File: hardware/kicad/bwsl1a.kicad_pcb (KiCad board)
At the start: 4 copper layers, 160 x 90 mm, 67 parts, among them J1 Conn_01x03, J11 USB_OTG, J13 USB_67298-4090, J14 Conn_02x05_Odd_Even, J17 Molex 470531000, J2 Conn_02x07_Odd_Even, J3 Conn_01x03, J9 THD-02-R, U1 TPD4EUSB30, U11 EMC2301-1-ACZL-TR, U13 FSUSB42MUX, U14 74LVC1G07SE-7, U2 TPD4EUSB30, U3 MagJack-A70-112-331N126, U4 TPD4EUSB30, U5 74LVC1G07SE-7, U6 USB2514B_Bi, U7 AP2553W6, U8 PCF85063AT/AAZ, U9 74LVC1G07SE-7, Y1 24MHz, Y2 X32K768S301

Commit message: initial pcb design
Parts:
- removed J11: USB_OTG, CM4IO:USB_Micro-B_EDAC_UCON00686
- removed J13: USB_67298-4090, CM4IO:MOLEX_USB_67298-4090
- removed J9: THD-02-R, Connector_PinHeader_2.54mm:PinHeader_2x02_P2.54mm_Vertical
- added C12: 0.1uF, Capacitor_SMD:C_0402_1005Metric, F.Cu at (103.2, 120.6)
- added C13: 10uF, Capacitor_SMD:C_0805_2012Metric, F.Cu at (105.1, 120.6)
- added C18: 0.1uF, Capacitor_SMD:C_0402_1005Metric, F.Cu at (107.0, 120.6)
- added C25: 100uF, Capacitor_SMD:C_1210_3225Metric, F.Cu at (100.7, 120.6)
- added C26: 100uF, Capacitor_SMD:C_1210_3225Metric, F.Cu at (188.7, 120.2)
- added C27: 0.1uF, Capacitor_SMD:C_0402_1005Metric, F.Cu at (186.2, 120.2)
- added C28: 10uF, Capacitor_SMD:C_0805_2012Metric, F.Cu at (184.1, 120.2)
- added C29: 0.1uF, Capacitor_SMD:C_0402_1005Metric, F.Cu at (182.1, 120.2)
- added C30: 100uF, Capacitor_SMD:C_1210_3225Metric, F.Cu at (179.6, 120.2)
- added C31: 10u, Capacitor_SMD:C_0805_2012Metric, F.Cu at (195.7, 127.5)
- added C32: 10u, Capacitor_SMD:C_0805_2012Metric, F.Cu at (193.7, 127.5)
- added C33: 10u, Capacitor_SMD:C_0805_2012Metric, F.Cu at (193.7, 131.0)
- added C34: 10u, Capacitor_SMD:C_0805_2012Metric, F.Cu at (195.7, 131.0)
- added C35: 100uF, Capacitor_Tantalum_SMD:CP_EIA-7343-31_Kemet-D, F.Cu at (190.1, 129.3)
- added C36: 10u, Capacitor_SMD:C_0805_2012Metric, F.Cu at (99.3, 131.7)
- added C37: 10u, Capacitor_SMD:C_0805_2012Metric, F.Cu at (171.3, 124.8)
- added C38: 10u, Capacitor_SMD:C_0805_2012Metric, F.Cu at (97.3, 131.7)
- added C39: 10u, Capacitor_SMD:C_0805_2012Metric, F.Cu at (167.8, 126.9)
- added C40: 10u, Capacitor_SMD:C_0805_2012Metric, F.Cu at (99.3, 128.1)
- added C41: 10u, Capacitor_SMD:C_0805_2012Metric, F.Cu at (167.8, 124.8)
- added C42: 10u, Capacitor_SMD:C_0805_2012Metric, F.Cu at (97.3, 128.1)
- added C43: 10u, Capacitor_SMD:C_0805_2012Metric, F.Cu at (171.3, 126.9)
- added C44: 100uF, Capacitor_Tantalum_SMD:CP_EIA-7343-31_Kemet-D, F.Cu at (102.9, 130.4)
- added C45: 100uF, Capacitor_Tantalum_SMD:CP_EIA-7343-31_Kemet-D, F.Cu at (169.7, 121.4)
- added C5: 100uF, Capacitor_SMD:C_1210_3225Metric, F.Cu at (109.6, 120.6)
- added G***: LOGO, Teapot:TeapotLogo, F.Cu at (127.5, 116.5)
- added G***: LOGO, Teapot:TeapotLogo, B.Cu at (186.9, 92.7)
- added G***: LOGO, Teapot:TextLogo_Teapot, B.Cu at (190.4, 98.1)
- added G***: LOGO, Teapot:TextLogo_BWSL1A, B.Cu at (182.6, 97.8)
- added G***: LOGO, Teapot:TextLogo_DataBoard, B.Cu at (186.1, 100.7)
- added H1: MountingHole, MountingHole:MountingHole_3mm_Pad_Via, F.Cu at (92.1, 72.4)
- added H2: MountingHole, MountingHole:MountingHole_3mm_Pad_Via, F.Cu at (198.7, 72.4)
- added H3: MountingHole, MountingHole:MountingHole_3mm_Pad_Via, F.Cu at (198.7, 139.7)
- added H4: MountingHole, MountingHole:MountingHole_3mm_Pad_Via, F.Cu at (92.1, 139.7)
- added J4: 5V, Connector_Wire:SolderWire-0.5sqmm_1x02_P4.8mm_D0.9mm_OD2.3mm, F.Cu at (166.9, 135.1)
- added J5: USB_67298-4090, Teapot:MOLEX_USB_67298-4090, F.Cu at (138.1, 137.9)
- added J6: 12V, Connector_Wire:SolderWire-0.5sqmm_1x02_P4.8mm_D0.9mm_OD2.3mm, F.Cu at (184.5, 128.4)
- added J7: USB_OTG, Teapot:USB_Micro-B_EDAC_UCON00686, F.Cu at (153.1, 145.5)
- added JP1: WL_DISABLE, Jumper:SolderJumper-2_P1.3mm_Open_RoundedPad1.0x1.5mm, F.Cu at (148.3, 74.8)
- added JP2: BT_DISABLE, Jumper:SolderJumper-2_P1.3mm_Open_RoundedPad1.0x1.5mm, F.Cu at (148.3, 78.7)
- added JP3: EEPROM_WP, Jumper:SolderJumper-2_P1.3mm_Open_RoundedPad1.0x1.5mm, F.Cu at (153.4, 90.7)
- added JP4: USB_BOOT, Jumper:SolderJumper-2_P1.3mm_Open_RoundedPad1.0x1.5mm, F.Cu at (148.3, 71.0)
- added R17: 0R, Resistor_SMD:R_0402_1005Metric, F.Cu at (156.3, 82.5)
- added R18: 0R, Resistor_SMD:R_0402_1005Metric, F.Cu at (156.3, 84.6)
- added R22: 0R, Resistor_SMD:R_0402_1005Metric, F.Cu at (156.3, 83.6)
- added R23: 2.2K 1%, Resistor_SMD:R_0402_1005Metric, F.Cu at (156.3, 79.9)
- added R24: 2.2K 1%, Resistor_SMD:R_0402_1005Metric, F.Cu at (156.3, 80.9)
- added R6: 0R, Resistor_SMD:R_0402_1005Metric, F.Cu at (156.3, 87.6)
- added R7: 0R, Resistor_SMD:R_0402_1005Metric, F.Cu at (156.3, 86.6)
- added R9: 0R, Resistor_SMD:R_0402_1005Metric, F.Cu at (156.3, 85.6)
- added SW1: Wake, Button_Switch_SMD:SW_SPST_TL3342, F.Cu at (177.0, 130.9)
- added TP1: ~, TestPoint:TestPoint_Pad_D1.0mm, F.Cu at (178.8, 137.1)
- added TP10: GLOBAL_EN, TestPoint:TestPoint_Pad_D1.0mm, B.Cu at (117.2, 71.6)
- added TP11: GND, TestPoint:TestPoint_Pad_D1.0mm, B.Cu at (137.9, 83.3)
- added TP12: 3.3v, TestPoint:TestPoint_Pad_D1.0mm, B.Cu at (155.7, 76.8)
- added TP13: TXD0, TestPoint:TestPoint_Pad_D1.0mm, B.Cu at (165.2, 80.5)
- added TP14: RXD0, TestPoint:TestPoint_Pad_D1.0mm, B.Cu at (165.1, 82.9)
- added TP15: GND, TestPoint:TestPoint_Pad_D1.0mm, B.Cu at (167.6, 83.7)
- added TP16: GPS_RESET, TestPoint:TestPoint_Pad_D1.0mm, B.Cu at (104.9, 117.4)
- added TP17: GPS_STANDBY, TestPoint:TestPoint_Pad_D1.0mm, B.Cu at (107.5, 117.4)
- added TP18: GPS_RXD, TestPoint:TestPoint_Pad_D1.0mm, B.Cu at (110.0, 117.4)
- added TP19: GPS_TXD, TestPoint:TestPoint_Pad_D1.0mm, B.Cu at (112.5, 117.4)
- added TP2: AIN0, TestPoint:TestPoint_Pad_D1.0mm, B.Cu at (153.7, 65.5)
- added TP20: GND, TestPoint:TestPoint_Pad_D1.0mm, B.Cu at (115.1, 117.4)
- added TP21: 3.3v LoRaWAN, TestPoint:TestPoint_Pad_D1.0mm, F.Cu at (93.0, 134.4)
- added TP22: 3.3v SWARM, TestPoint:TestPoint_Pad_D1.0mm, F.Cu at (193.8, 120.6)
- added TP23: 5v, TestPoint:TestPoint_Pad_D1.0mm, F.Cu at (162.7, 129.0)
- added TP24: 12v, TestPoint:TestPoint_Pad_D1.0mm, F.Cu at (187.6, 135.5)
- added TP25: GND, TestPoint:TestPoint_Pad_D1.0mm, F.Cu at (177.4, 124.2)
- added TP26: GND, TestPoint:TestPoint_Pad_D1.0mm, F.Cu at (94.1, 120.0)
- added TP4: AIN1, TestPoint:TestPoint_Pad_D1.0mm, B.Cu at (153.8, 67.9)
- added TP6: SYNC_IN, TestPoint:TestPoint_Pad_D1.0mm, B.Cu at (155.8, 90.2)
- added TP7: SYNC_OUT, TestPoint:TestPoint_Pad_D1.0mm, B.Cu at (153.5, 89.8)
- added TP8: TV_OUT, TestPoint:TestPoint_Pad_D1.0mm, B.Cu at (132.6, 90.4)
- added TP9: RUN_PG, TestPoint:TestPoint_Pad_D1.0mm, B.Cu at (168.8, 73.4)
- added U10: RAK5146, Teapot:RAK5146, F.Cu at (106.4, 110.4)
- added U12: Swarm_M138, Teapot:Swarm_M138, F.Cu at (183.9, 110.4)
- BT1, C22, C24, C46, D3, R19, R20, U14, U8, Y2: moved to B.Cu
- J1: value Conn_01x03 -> 3.3V LoRaWAN; footprint Connector_PinHeader_2.54mm:PinHeader_1x03_P2.54mm_Vertical -> Connector_Wire:SolderWire-0.5sqmm_1x02_P4.8mm_D0.9mm_OD2.3mm
- J2: value Conn_02x07_Odd_Even -> 3.3V SWARM; footprint Connector_PinHeader_2.54mm:PinHeader_2x07_P2.54mm_Vertical -> Connector_Wire:SolderWire-0.5sqmm_1x02_P4.8mm_D0.9mm_OD2.3mm
- J3: value Conn_01x03 -> BMS I2C; footprint Connector_PinHeader_2.54mm:PinHeader_1x03_P2.54mm_Vertical -> Connector_PinHeader_2.54mm:PinHeader_1x04_P2.54mm_Vertical; moved to B.Cu
- U3: footprint CM4IO:TRJG0926HENL -> Teapot:TRJG0926HENL
- moved J3 84.4 mm to (161.9, 143.5), turned to 0 degrees
- moved J17 79.4 mm to (183.9, 140.6)
- moved J2 77.6 mm to (199.4, 123.2), turned to -90 degrees
- moved C23 71.9 mm to (170.4, 141.6)
- moved U11 71.9 mm to (174.8, 140.7)
- moved R21 71.9 mm to (174.7, 143.4)
- moved U9 59.2 mm to (175.0, 137.1), turned to 0 degrees
- moved C46 46.8 mm to (97.1, 78.3)
- moved Y2 42.3 mm to (105.2, 80.6), turned to -90 degrees
- moved R19 41.3 mm to (112.3, 77.8), turned to 180 degrees
- moved C24 40.6 mm to (112.8, 79.3), turned to 90 degrees
- moved U8 39.3 mm to (99.3, 82.2)
- moved R20 39.2 mm to (112.3, 80.9), turned to 180 degrees
- moved U14 38.0 mm to (112.9, 83.4), turned to -90 degrees
- moved C22 36.9 mm to (110.8, 83.7), turned to 90 degrees
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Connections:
- C10 pad 1: /USB/+3.3v -> /+3.3v
- C11 pad 1: /USB/+3.3v -> /+3.3v
- C14 pad 1: /USB/+3.3v -> /+3.3v
- C15 pad 1: /USB/+3.3v -> /+3.3v
- C2 pad 1: /USB/+5v -> /+5v
- C22 pad 1: /RTC_Fan/+5v -> /+5v
- C23 pad 1: /RTC_Fan/+3.3v -> /+3.3v
- C3 pad 1: /USB/+3.3v -> /+3.3v
- C4 pad 1: /USB/+3.3v -> /+3.3v
- C6 pad 1: /USB/+3.3v -> /+3.3v
- C7 pad 1: /USB/+3.3v -> /+3.3v
- D1 pad 2: /Ethernet/+3.3v -> /+3.3v
- D2 pad 2: /Ethernet/+3.3v -> /+3.3v
- D3 pad 2: /RTC_Fan/+3.3v -> /+3.3v
- J1 pad 1: /Ethernet/GLOBAL_EN -> GND
- J1 pad 2: GND -> /+3.3vL
- J17 pad 2: /RTC_Fan/+12v -> /+12v
- J2 pad 2: /Ethernet/nRPIBOOT -> /+3.3vS
- J3 pad 1: /Ethernet/WL_nDis -> GND
- J3 pad 2: GND -> /SCL1
- J3 pad 3: /Ethernet/BT_nDis -> /SDA1
- Module1 pad 1: (no net) -> GND
- Module1 pad 10: (no net) -> /IO_Ethernet/TRD0_N
- Module1 pad 100: (no net) -> /USB/nEXTRST
- Module1 pad 11: (no net) -> /IO_Ethernet/TRD2_P
- Module1 pad 111: unconnected-(Module1-Pad111) -> /IO_Ethernet/TV_OUT
- Module1 pad 12: (no net) -> /IO_Ethernet/TRD0_P
- Module1 pad 13: (no net) -> GND
- Module1 pad 14: (no net) -> GND
- Module1 pad 15: (no net) -> /IO_Ethernet/ETH_LEDY
- Module1 pad 16: (no net) -> /IO_Ethernet/SYNC_IN
- Module1 pad 17: (no net) -> /IO_Ethernet/ETH_LEDG
- Module1 pad 18: (no net) -> /IO_Ethernet/SYNC_OUT
- Module1 pad 19: (no net) -> unconnected-(Module1-Pad19)
- Module1 pad 2: (no net) -> GND
- Module1 pad 20: (no net) -> /IO_Ethernet/EEPROM_nWP
- Module1 pad 21: (no net) -> Net-(Module1-Pad21)
- Module1 pad 22: (no net) -> GND
- Module1 pad 23: (no net) -> GND
- Module1 pad 24: (no net) -> Net-(Module1-Pad24)
- Module1 pad 25: (no net) -> unconnected-(Module1-Pad25)
- Module1 pad 26: (no net) -> Net-(Module1-Pad26)
- Module1 pad 27: (no net) -> unconnected-(Module1-Pad27)
- Module1 pad 28: (no net) -> Net-(Module1-Pad28)
- Module1 pad 29: (no net) -> unconnected-(Module1-Pad29)
- Module1 pad 3: (no net) -> /IO_Ethernet/TRD3_P
- Module1 pad 30: (no net) -> unconnected-(Module1-Pad30)
- Module1 pad 31: (no net) -> unconnected-(Module1-Pad31)
- Module1 pad 32: (no net) -> GND
- Module1 pad 33: (no net) -> GND
- Module1 pad 34: (no net) -> /SWARM_TXD
- Module1 pad 35: (no net) -> /IO_Ethernet/ID_SC
- Module1 pad 36: (no net) -> /IO_Ethernet/ID_SD
- Module1 pad 37: (no net) -> unconnected-(Module1-Pad37)
- Module1 pad 38: (no net) -> /LORA_SCK
- Module1 pad 39: (no net) -> /LORA_CSN
- Module1 pad 4: (no net) -> /IO_Ethernet/TRD1_P
- Module1 pad 40: (no net) -> /LORA_MISO
- Module1 pad 41: (no net) -> Net-(Module1-Pad41)
- Module1 pad 42: (no net) -> GND
- Module1 pad 43: (no net) -> GND
- Module1 pad 44: (no net) -> /LORA_MOSI
- Module1 pad 45: (no net) -> Net-(Module1-Pad45)
- Module1 pad 46: (no net) -> unconnected-(Module1-Pad46)
- Module1 pad 47: (no net) -> unconnected-(Module1-Pad47)
- Module1 pad 48: (no net) -> unconnected-(Module1-Pad48)
- Module1 pad 49: (no net) -> unconnected-(Module1-Pad49)
- Module1 pad 5: (no net) -> /IO_Ethernet/TRD3_N
- Module1 pad 50: (no net) -> Net-(Module1-Pad50)
- Module1 pad 51: (no net) -> /IO_Ethernet/RXD0
- Module1 pad 52: (no net) -> GND
- Module1 pad 53: (no net) -> GND
- Module1 pad 54: (no net) -> /SWARM_RXD
- Module1 pad 55: (no net) -> /IO_Ethernet/TXD0
- Module1 pad 56: (no net) -> /SCL1
- Module1 pad 57: (no net) -> unconnected-(Module1-Pad57)
- Module1 pad 58: (no net) -> /SDA1
- Module1 pad 59: (no net) -> GND
- Module1 pad 6: (no net) -> /IO_Ethernet/TRD1_N
- Module1 pad 60: (no net) -> GND
- Module1 pad 61: (no net) -> unconnected-(Module1-Pad61)
- Module1 pad 62: (no net) -> unconnected-(Module1-Pad62)
- Module1 pad 63: (no net) -> unconnected-(Module1-Pad63)
- Module1 pad 64: (no net) -> unconnected-(Module1-Pad64)
- Module1 pad 65: (no net) -> GND
- Module1 pad 66: (no net) -> GND
- Module1 pad 67: (no net) -> unconnected-(Module1-Pad67)
- Module1 pad 68: (no net) -> unconnected-(Module1-Pad68)
- Module1 pad 69: (no net) -> unconnected-(Module1-Pad69)
- Module1 pad 7: (no net) -> GND
- Module1 pad 70: (no net) -> unconnected-(Module1-Pad70)
- Module1 pad 71: (no net) -> GND
- Module1 pad 72: (no net) -> unconnected-(Module1-Pad72)
- Module1 pad 73: (no net) -> unconnected-(Module1-Pad73)
- Module1 pad 74: (no net) -> GND
- Module1 pad 75: (no net) -> unconnected-(Module1-Pad75)
- Module1 pad 76: (no net) -> /IO_Ethernet/Reserved
- Module1 pad 77: (no net) -> /+5v
- Module1 pad 78: (no net) -> /IO_Ethernet/GPIO_VREF
- Module1 pad 79: (no net) -> /+5v
- Module1 pad 8: (no net) -> GND
- Module1 pad 80: (no net) -> unconnected-(Module1-Pad80)
- Module1 pad 81: (no net) -> /+5v
- Module1 pad 82: (no net) -> unconnected-(Module1-Pad82)
- Module1 pad 83: (no net) -> /+5v
- Module1 pad 84: (no net) -> /+3.3v
- Module1 pad 85: (no net) -> /+5v
- Module1 pad 86: (no net) -> /+3.3v
- Module1 pad 87: (no net) -> /+5v
- Module1 pad 88: (no net) -> /IO_Ethernet/+1.8v
- Module1 pad 89: (no net) -> /IO_Ethernet/WL_nDis
- Module1 pad 9: (no net) -> /IO_Ethernet/TRD2_N
- Module1 pad 90: (no net) -> /IO_Ethernet/+1.8v
- Module1 pad 91: (no net) -> /IO_Ethernet/BT_nDis
- Module1 pad 92: (no net) -> /IO_Ethernet/RUN_PG
- Module1 pad 93: (no net) -> /IO_Ethernet/nRPIBOOT
- Module1 pad 94: (no net) -> /IO_Ethernet/AIN1
- Module1 pad 95: (no net) -> /IO_Ethernet/nPWR_LED
- Module1 pad 96: (no net) -> /IO_Ethernet/AIN0
- Module1 pad 97: (no net) -> unconnected-(Module1-Pad97)
- Module1 pad 98: (no net) -> GND
- Module1 pad 99: (no net) -> /IO_Ethernet/GLOBAL_EN
- R1 pad 2: Net-(R1-Pad2) -> Net-(Module1-Pad21)
- R19 pad 2: /RTC_Fan/+5v -> /+5v
- R2 pad 2: /Ethernet/ETH_LEDG -> /IO_Ethernet/ETH_LEDG
- R20 pad 2: /RTC_Fan/+5v -> /+5v
- R21 pad 2: /RTC_Fan/+3.3v -> /+3.3v
- R3 pad 2: /Ethernet/ETH_LEDY -> /IO_Ethernet/ETH_LEDY
- R4 pad 1: /Ethernet/+1.8v -> /IO_Ethernet/+1.8v
- R4 pad 2: /Ethernet/GPIO_VREF -> /IO_Ethernet/GPIO_VREF
- R5 pad 1: /Ethernet/+3.3v -> /+3.3v
- R5 pad 2: /Ethernet/GPIO_VREF -> /IO_Ethernet/GPIO_VREF
- R8 pad 1: /USB/USB_OTG_ID -> Net-(J7-Pad1)
- R8 pad 2: Net-(J11-Pad1) -> /USB/USB_OTG_ID
- U1 pad 1: /Ethernet/TRD3_P -> /IO_Ethernet/TRD3_P
- U1 pad 10: unconnected-(U1-Pad10) -> /IO_Ethernet/TRD3_P
- U1 pad 2: /Ethernet/TRD3_N -> /IO_Ethernet/TRD3_N
- U1 pad 4: /Ethernet/TRD2_N -> /IO_Ethernet/TRD2_N
- U1 pad 5: /Ethernet/TRD2_P -> /IO_Ethernet/TRD2_P
- U1 pad 6: unconnected-(U1-Pad6) -> /IO_Ethernet/TRD2_P
- U1 pad 7: unconnected-(U1-Pad7) -> /IO_Ethernet/TRD2_N
- U1 pad 9: unconnected-(U1-Pad9) -> /IO_Ethernet/TRD3_N
- U11 pad 1: /RTC_Fan/SDA -> /SDA1
- U11 pad 2: /RTC_Fan/SCL -> /SCL1
- U11 pad 3: /RTC_Fan/+3.3v -> /+3.3v
- U13 pad 1: /USB/+3.3v -> /+3.3v
- U13 pad 6: /USB/USBH_P -> /USB/USBH_N
- U13 pad 7: /USB/USBH_N -> /USB/USBH_P
- U14 pad 4: /RTC_Fan/GLOBAL_EN -> /IO_Ethernet/GLOBAL_EN
- U14 pad 5: /RTC_Fan/+5v -> /+5v
- U2 pad 1: /Ethernet/TRD1_P -> /IO_Ethernet/TRD1_P
- U2 pad 10: unconnected-(U2-Pad10) -> /IO_Ethernet/TRD1_P
- U2 pad 2: /Ethernet/TRD1_N -> /IO_Ethernet/TRD1_N
- U2 pad 4: /Ethernet/TRD0_N -> /IO_Ethernet/TRD0_N
- U2 pad 5: /Ethernet/TRD0_P -> /IO_Ethernet/TRD0_P
- U2 pad 6: unconnected-(U2-Pad6) -> /IO_Ethernet/TRD0_P
- U2 pad 7: unconnected-(U2-Pad7) -> /IO_Ethernet/TRD0_N
- U2 pad 9: unconnected-(U2-Pad9) -> /IO_Ethernet/TRD1_N
- U3 pad 1: /Ethernet/TRD0_P -> /IO_Ethernet/TRD0_P
- U3 pad 10: /Ethernet/TRD3_N -> /IO_Ethernet/TRD3_N
- U3 pad 11: /Ethernet/TR0_TAP -> /IO_Ethernet/TR0_TAP
- U3 pad 12: /Ethernet/TR1_TAP -> /IO_Ethernet/TR1_TAP
- U3 pad 13: /Ethernet/TR2_TAP -> /IO_Ethernet/TR2_TAP
- U3 pad 14: /Ethernet/TR3_TAP -> /IO_Ethernet/TR3_TAP
- U3 pad 15: /Ethernet/+3.3v -> /+3.3v
- U3 pad 17: /Ethernet/+3.3v -> /+3.3v
- U3 pad 2: /Ethernet/TRD0_N -> /IO_Ethernet/TRD0_N
- U3 pad 3: /Ethernet/TRD1_P -> /IO_Ethernet/TRD1_P
- U3 pad 6: /Ethernet/TRD1_N -> /IO_Ethernet/TRD1_N
- U3 pad 7: /Ethernet/TRD2_P -> /IO_Ethernet/TRD2_P
- U3 pad 8: /Ethernet/TRD2_N -> /IO_Ethernet/TRD2_N
- U3 pad 9: /Ethernet/TRD3_P -> /IO_Ethernet/TRD3_P
- U4 pad 1: unconnected-(U4-Pad1) -> Net-(U4-Pad1)
- U4 pad 10: unconnected-(U4-Pad10) -> Net-(U4-Pad1)
- U4 pad 2: unconnected-(U4-Pad2) -> Net-(U4-Pad2)
- U4 pad 6: unconnected-(U4-Pad6) -> /USB/USBD_P
- U4 pad 7: unconnected-(U4-Pad7) -> /USB/USBD_N
- U4 pad 9: unconnected-(U4-Pad9) -> Net-(U4-Pad2)
- U5 pad 2: /Ethernet/nPWR_LED -> /IO_Ethernet/nPWR_LED
- U5 pad 5: /Ethernet/+3.3v -> /+3.3v
- U6 pad 10: /USB/+3.3v -> /+3.3v
- U6 pad 15: /USB/+3.3v -> /+3.3v
- U6 pad 23: /USB/+3.3v -> /+3.3v
- U6 pad 27: /USB/+3.3v -> /+3.3v
- U6 pad 29: /USB/+3.3v -> /+3.3v
- U6 pad 36: /USB/+3.3v -> /+3.3v
- U6 pad 5: /USB/+3.3v -> /+3.3v
- U7 pad 1: /USB/+5v -> /+5v
- U8 pad 5: /RTC_Fan/SDA -> /SDA1
- U8 pad 6: /RTC_Fan/SCL -> /SCL1
- U9 pad 2: /Ethernet/RUN_PG -> /IO_Ethernet/RUN_PG
- U9 pad 4: Net-(J2-Pad13) -> Net-(SW1-Pad1)
- U9 pad 5: /Ethernet/+5v -> /+5v
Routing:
- net /USB/+3.3v: track 449.6 -> 0.00 mm, vias 23 -> 0
- net /+3.3v: track 0.00 -> 312.9 mm, vias 0 -> 25
- net /RTC_Fan/+5v: track 262.7 -> 0.00 mm, vias 20 -> 0
- net /SCL1: track 0.00 -> 202.6 mm, vias 0 -> 5
- net /RTC_Fan/SCL: track 201.2 -> 0.00 mm, vias 8 -> 0
- net /SDA1: track 0.00 -> 200.2 mm, vias 0 -> 8
- net /Ethernet/GLOBAL_EN: track 196.2 -> 0.00 mm, vias 5 -> 0
- net /RTC_Fan/SDA: track 194.6 -> 0.00 mm, vias 8 -> 0
- net /+5v: track 0.00 -> 188.0 mm, vias 0 -> 13
- net /Ethernet/RUN_PG: track 170.6 -> 0.00 mm, vias 4 -> 0
- net /IO_Ethernet/GLOBAL_EN: track 0.00 -> 135.5 mm, vias 0 -> 5
- net /Ethernet/nPWR_LED: track 128.9 -> 0.00 mm, vias 2 -> 0
- net Net-(R1-Pad2): track 116.6 -> 0.00 mm, vias 4 -> 0
- net /IO_Ethernet/nPWR_LED: track 0.00 -> 113.2 mm, vias 0 -> 4
- net /+3.3vL: track 0.00 -> 101.9 mm
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- added copper zone on In2.Cu, net /+3.3v
- added copper zone on B.Cu, net GND
- added copper zone on F.Cu, net GND
- added copper zone on In1.Cu, net GND
- added copper zone on In2.Cu, net GND
- removed copper zone on In2.Cu, net /USB/+3.3v
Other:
- board size 160 x 90 mm -> 120 x 90 mm
- board text added: "+"
- board text added: "-"
- board text added: "RAK5146 LoRaWAN Concentrator"
- board text added: "SWARM M138 Transceiver"
- board text removed: "Battery CR2032"
- board text removed: "Board thickness : 1.56mm Finished copper weight inners : 1oz Finished copper weight outers : 1oz Board finish : OSP Material type : FR4 Colour of solder resists : Green Colour of silk screens : White Only on the top side Board to : UL94-V0 TG >=130 50R trace width 0.13mm@ 3GHz 90R diff pair width 0.147 spacing 0.253mm @ 2.5GHz 100R diff pair width 0.127 spacing 0.253mm @ 2GHz"
- board text removed: "FAN"
- board text removed: "Fit jumper to disable eMMC Boot"
- board text removed: "Fit jumper to disable writing to EEPROM"
- board text removed: "J3 : nBT_Dis GND"
- board text removed: "PCIe x1"
- board text removed: "POE"
- board text removed: "RUN GLOBAL_EN"
- board text removed: "Rev 5b"
- board text removed: "nWireless_Dis"

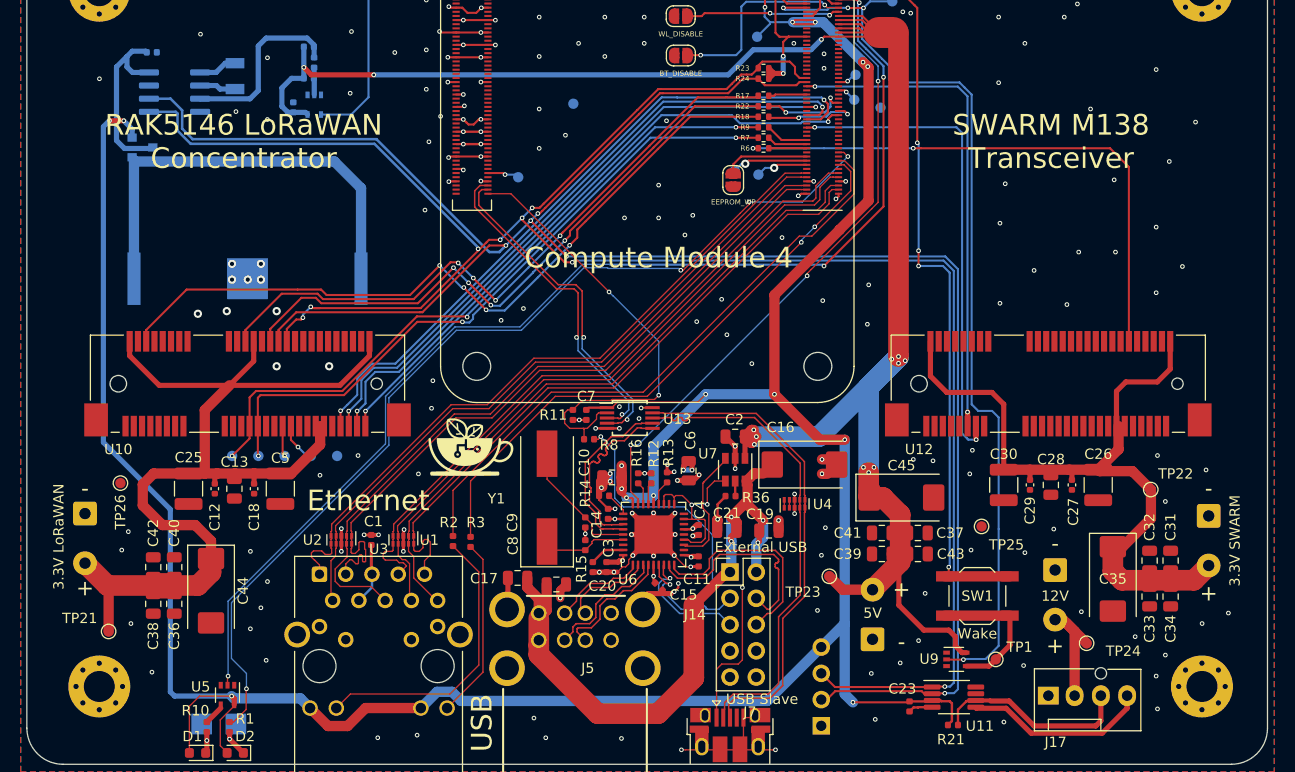
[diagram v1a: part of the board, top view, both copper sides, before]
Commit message: move power capacitor to bottom layer
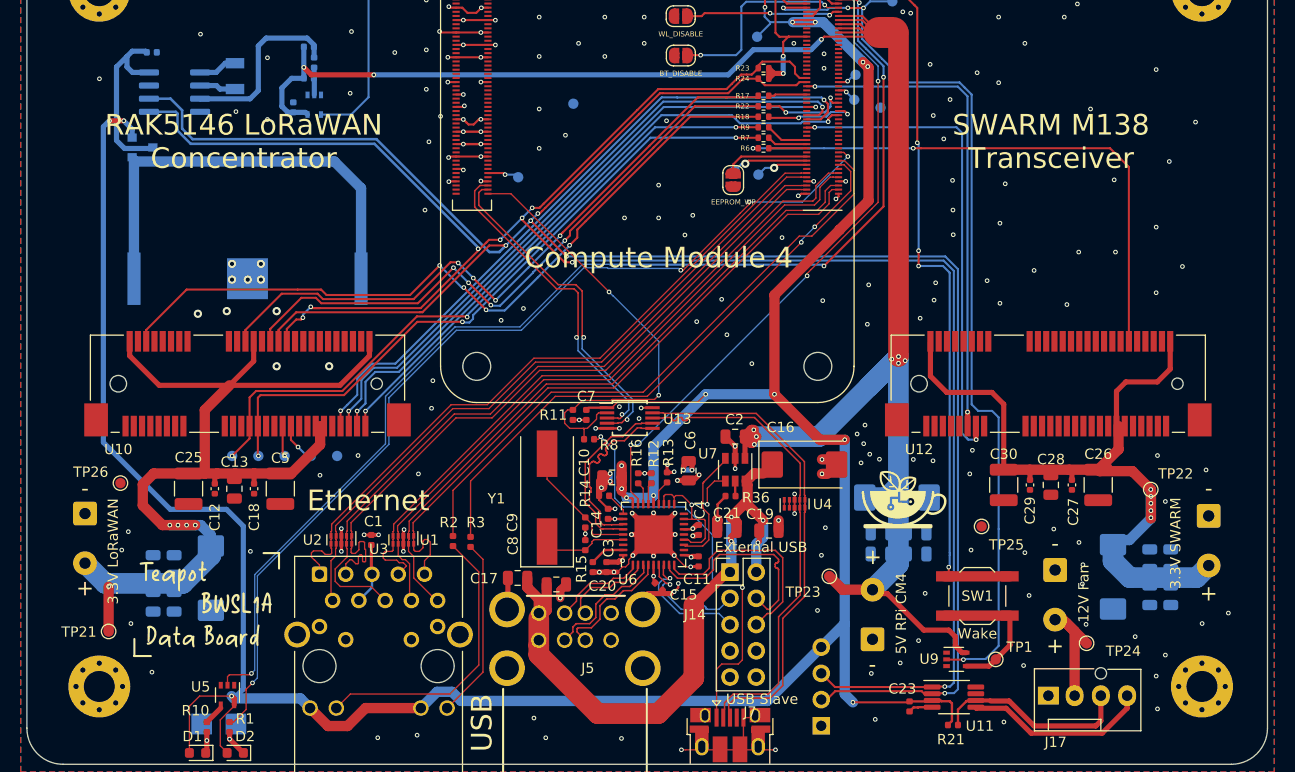
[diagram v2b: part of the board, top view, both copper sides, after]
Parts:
- added G***: LOGO, Teapot:TextLogo_Teapot, F.Cu at (99.4, 129.1)
- added G***: LOGO, Teapot:TextLogo_BWSL1A, F.Cu at (105.3, 131.6)
- added G***: LOGO, Teapot:TextLogo_DataBoard, F.Cu at (102.2, 134.8)
- C31, C32, C33, C34, C35, C36, C37, C38, C39, C40, C41, C42, C43, C44, C45: moved to B.Cu
- J4: value 5V -> 5V RPi CM4
- J6: value 12V -> 12V Fan
- moved G*** 42.2 mm to (169.5, 121.5)
- moved C36 3.76 mm to (99.3, 127.9), turned to 90 degrees
- moved C38 3.76 mm to (97.3, 127.9), turned to 90 degrees
- moved C43 3.62 mm to (167.6, 126.9), turned to 180 degrees
- moved C33 3.62 mm to (193.7, 127.4), turned to 90 degrees
- moved C34 3.62 mm to (195.7, 127.4), turned to 90 degrees
- moved C37 3.61 mm to (167.6, 124.8), turned to 180 degrees
- moved C39 3.37 mm to (171.1, 126.9), turned to 0 degrees
- moved C41 3.37 mm to (171.1, 124.8), turned to 0 degrees
- moved C31 3.35 mm to (195.7, 130.9), turned to -90 degrees
- moved C32 3.35 mm to (193.7, 130.9), turned to -90 degrees
- moved C40 3.35 mm to (99.3, 131.5), turned to -90 degrees
- moved C42 3.35 mm to (97.3, 131.5), turned to -90 degrees
- moved C44 1.22 mm to (102.9, 129.2)
- moved C45 0.44 mm to (169.2, 121.4)
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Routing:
- net /+3.3vS: track 72.4 -> 74.6 mm, vias 0 -> 5
- net /+3.3vL: track 101.9 -> 99.8 mm, vias 0 -> 5
- net /+5v: track 188.0 -> 189.3 mm, vias 13 -> 10
- net Net-(Module1-Pad21): track 94.7 -> 93.5 mm
- net /IO_Ethernet/nPWR_LED: track 113.2 -> 114.4 mm
- net /+3.3v: track 312.9 -> 313.9 mm
- net GND: track 133.1 -> 133.2 mm, vias 211 -> 229
